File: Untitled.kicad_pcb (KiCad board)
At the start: 2 copper layers, 111.8 x 37.5 mm, 28 parts, among them J1 JAMMA, J2 CONN_01X06, J5 PWR_IN, J6 DC2DC, J7 SCART-F, SW1 SW_Push, SW2 SW_Push, SW3 SW_Push, U1 LD1117S33TR, U2 ESP32-WROOM, U3 TLC5926IDW, U4 TLC5926IDW

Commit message: Lynn almost done
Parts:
- removed C1, C2, C3: 4.7u, Capacitors_SMD:C_1206_HandSoldering
- removed J5: PWR_IN, Connectors:BARREL_JACK
- removed J6: DC2DC, NQR010A0X4Z:NQR010A0X4Z
- removed J7: SCART-F, w_conn_av:SCART
- removed R10: 100, Resistors_SMD:R_1206_HandSoldering
- removed R3, R4: 330, Resistors_SMD:R_1206_HandSoldering
- removed R5: 10K, Resistors_SMD:R_1206_HandSoldering
- removed R6: 1K, Resistors_SMD:R_1206_HandSoldering
- removed R7: 240, Resistors_SMD:R_1206_HandSoldering
- removed R8: 500, Potentiometers:Potentiometer_Bourns_3296W_3-8Zoll_Inline_ScrewUp
- removed R9: 33, Resistors_SMD:R_1206_HandSoldering
- removed SW1, SW2, SW3: SW_Push, Buttons_Switches_SMD:SW_SPST_EVQPE1
- added D1: LED, LEDs:LED_1206_HandSoldering, F.Cu at (241.2, 94.2)
- added D10: LED, LEDs:LED_1206_HandSoldering, F.Cu at (214.8, 100.2)
- added D11: LED, LEDs:LED_1206_HandSoldering, F.Cu at (231.2, 101.1)
- added D12: LED, LEDs:LED_1206_HandSoldering, F.Cu at (237.7, 98.7)
- added D13: LED, LEDs:LED_1206_HandSoldering, F.Cu at (223.1, 84.7)
- added D14: LED, LEDs:LED_1206_HandSoldering, F.Cu at (225.3, 78.6)
- added D15: LED, LEDs:LED_1206_HandSoldering, F.Cu at (205.2, 96.0)
- added D16: LED, LEDs:LED_1206_HandSoldering, F.Cu at (207.4, 89.8)
- added D17: LED, LEDs:LED_1206_HandSoldering, F.Cu at (197.5, 85.0)
- added D18: LED, LEDs:LED_1206_HandSoldering, F.Cu at (200.9, 78.7)
- added D19: LED, LEDs:LED_1206_HandSoldering, F.Cu at (205.2, 81.5)
- added D2: LED, LEDs:LED_1206_HandSoldering, F.Cu at (234.6, 78.6)
- added D20: LED, LEDs:LED_1206_HandSoldering, F.Cu at (210.6, 78.8)
- added D21: LED, LEDs:LED_1206_HandSoldering, F.Cu at (210.3, 84.9)
- added D22: LED, LEDs:LED_1206_HandSoldering, F.Cu at (195.7, 90.2)
- added D23: LED, LEDs:LED_1206_HandSoldering, F.Cu at (192.2, 96.0)
- added D24: LED, LEDs:LED_1206_HandSoldering, F.Cu at (185.2, 100.8)
- added D25: LED, LEDs:LED_1206_HandSoldering, F.Cu at (178.5, 104.0)
- added D26: LED, LEDs:LED_1206_HandSoldering, F.Cu at (170.2, 107.0)
- added D27: LED, LEDs:LED_1206_HandSoldering, F.Cu at (164.9, 113.2)
- added D28: LED, LEDs:LED_1206_HandSoldering, F.Cu at (165.4, 122.5)
- added D29: LED, LEDs:LED_1206_HandSoldering, F.Cu at (171.2, 117.5)
- added D3: LED, LEDs:LED_1206_HandSoldering, F.Cu at (229.4, 81.3)
- added D30: LED, LEDs:LED_1206_HandSoldering, F.Cu at (175.4, 110.5)
- added D31: LED, LEDs:LED_1206_HandSoldering, F.Cu at (180.7, 97.2)
- added D32: LED, LEDs:LED_1206_HandSoldering, F.Cu at (183.7, 91.0)
- added D33: LED, LEDs:LED_1206_HandSoldering, F.Cu at (186.7, 85.2)
- added D34: LED, LEDs:LED_1206_HandSoldering, F.Cu at (189.2, 79.2)
- added D35: LED, LEDs:LED_1206_HandSoldering, F.Cu at (172.2, 100.5)
- added D36: LED, LEDs:LED_1206_HandSoldering, F.Cu at (169.2, 94.0)
- added D37: LED, LEDs:LED_1206_HandSoldering, F.Cu at (172.7, 87.8)
- added D38: LED, LEDs:LED_1206_HandSoldering, F.Cu at (176.4, 80.8)
- added D39: LED, LEDs:LED_1206_HandSoldering, F.Cu at (160.7, 98.2)
- added D4: LED, LEDs:LED_1206_HandSoldering, F.Cu at (234.7, 84.3)
- added D40: LED, LEDs:LED_1206_HandSoldering, F.Cu at (150.7, 100.0)
- added D41: LED, LEDs:LED_1206_HandSoldering, F.Cu at (148.9, 93.5)
- added D42: LED, LEDs:LED_1206_HandSoldering, F.Cu at (152.2, 86.8)
- added D43: LED, LEDs:LED_1206_HandSoldering, F.Cu at (155.4, 80.8)
- added D44: LED, LEDs:LED_1206_HandSoldering, F.Cu at (159.7, 74.0)
- added D45: LED, LEDs:LED_1206_HandSoldering, F.Cu at (162.9, 68.0)
- added D46: LED, LEDs:LED_1206_HandSoldering, B.Cu at (159.2, 90.2)
- added D47: LED, LEDs:LED_1206_HandSoldering, B.Cu at (159.2, 87.2)
- added D48: LED, LEDs:LED_1206_HandSoldering, B.Cu at (159.2, 84.2)
- added D5: LED, LEDs:LED_1206_HandSoldering, F.Cu at (231.4, 89.2)
- added D6: LED, LEDs:LED_1206_HandSoldering, F.Cu at (229.4, 95.4)
- added D7: LED, LEDs:LED_1206_HandSoldering, F.Cu at (220.2, 89.2)
- added D8: LED, LEDs:LED_1206_HandSoldering, F.Cu at (217.4, 94.5)
- added D9: LED, LEDs:LED_1206_HandSoldering, F.Cu at (206.6, 100.9)
- added U5: TLC5926IDW, Housings_SOIC:SOIC-24W_7.5x15.4mm_Pitch1.27mm, B.Cu at (172.8, 87.8)
- added lynn_outline: G***, svg2mod:lynn_outline, F.Cu at (175.0, 85.2)
- C4, R2, U1, U2, U3: moved to B.Cu
- J1: value JAMMA -> USB_B; footprint JAMMA:JAMMA -> Connectors:USB_Mini-B; moved to B.Cu
- R1: value 330 -> 10K; moved to B.Cu
- R11: value R -> 330; moved to B.Cu
- R12: value R -> 330
- moved C4 146.5 mm to (235.8, 102.3), turned to 0 degrees
- moved J2 142.8 mm to (228.7, 75.3), turned to 270 degrees
- moved U2 138.0 mm to (234.9, 89.4)
- moved R11 99.3 mm to (205.6, 77.7), turned to 0 degrees
- moved U3 94.9 mm to (205.7, 87.6), turned to 180 degrees
- moved R12 86.5 mm to (189.0, 77.0), turned to 0 degrees
- moved U4 82.8 mm to (189.6, 87.5), turned to 180 degrees
- moved J1 77.4 mm to (195.9, 101.2), turned to 90 degrees
- moved R2 74.3 mm to (172.8, 77.5), turned to 0 degrees
- moved R1 73.1 mm to (228.3, 102.3), turned to 180 degrees
- moved U1 49.5 mm to (176.7, 113.5)
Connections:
- J1 pad 1: GND -> +5V
- J1 pad 2: GND -> (no net)
- J1 pad 3: GND -> (no net)
- J1 pad 5: +5V -> (no net)
- J1 pad 6: +5V -> (no net)
- J2 pad 1: (no net) -> RESET
- J2 pad 5: (no net) -> PROG
- R1 pad 1: Net-(J7-Pad19) -> 33
- R1 pad 2: SYNC -> RESET
- R2 pad 2: Net-(C1-Pad2) -> GND
- U2 pad 25: Net-(SW3-Pad1) -> PROG
- U2 pad 29: LATCH -> (no net)
- U2 pad 3: Net-(SW2-Pad2) -> RESET
- U2 pad 30: CLK -> LATCH
- U2 pad 31: (no net) -> CLK
- U3 pad 10: LEFT1 -> Net-(D6-Pad1)
- U3 pad 11: DOWN1 -> Net-(D7-Pad1)
- U3 pad 12: UP1 -> Net-(D8-Pad1)
- U3 pad 13: TEST -> Net-(D9-Pad1)
- U3 pad 14: COIN1 -> Net-(D10-Pad1)
- U3 pad 15: START1 -> Net-(D11-Pad1)
- U3 pad 16: (no net) -> Net-(D12-Pad1)
- U3 pad 17: (no net) -> Net-(D13-Pad1)
- U3 pad 18: (no net) -> Net-(D14-Pad1)
- U3 pad 19: (no net) -> Net-(D15-Pad1)
- U3 pad 20: (no net) -> Net-(D16-Pad1)
- U3 pad 5: D1 -> Net-(D1-Pad1)
- U3 pad 6: C1 -> Net-(D2-Pad1)
- U3 pad 7: B1 -> Net-(D3-Pad1)
- U3 pad 8: A1 -> Net-(D4-Pad1)
- U3 pad 9: RIGHT1 -> Net-(D5-Pad1)
- U4 pad 10: START2 -> Net-(D22-Pad1)
- U4 pad 11: COIN2 -> Net-(D23-Pad1)
- U4 pad 12: SERVICE -> Net-(D24-Pad1)
- U4 pad 13: UP2 -> Net-(D25-Pad1)
- U4 pad 14: DOWN2 -> Net-(D26-Pad1)
- U4 pad 15: LEFT2 -> Net-(D27-Pad1)
- U4 pad 16: RIGHT2 -> Net-(D28-Pad1)
- U4 pad 17: A2 -> Net-(D29-Pad1)
- U4 pad 18: B2 -> Net-(D30-Pad1)
- U4 pad 19: C2 -> Net-(D31-Pad1)
- U4 pad 20: D2 -> Net-(D32-Pad1)
- U4 pad 22: (no net) -> Net-(U4-Pad22)
- U4 pad 5: (no net) -> Net-(D17-Pad1)
- U4 pad 6: (no net) -> Net-(D18-Pad1)
- U4 pad 7: (no net) -> Net-(D19-Pad1)
- U4 pad 8: (no net) -> Net-(D20-Pad1)
- U4 pad 9: (no net) -> Net-(D21-Pad1)
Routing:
- net +5V: track 126.2 -> 331.6 mm, vias 2 -> 3
- net GND: track 312.1 -> 162.7 mm, vias 5 -> 2
- net 33: track 77.8 -> 153.4 mm, vias 3 -> 0
- net +12V: track 69.1 -> 0.00 mm, vias 2 -> 0
- net Net-(D1-Pad1): track 0.00 -> 67.3 mm, vias 0 -> 1
- net RESET: track 0.00 -> 64.2 mm
- net Net-(D12-Pad1): track 0.00 -> 53.3 mm, vias 0 -> 1
- net VIDEO_GND: track 51.1 -> 0.00 mm, vias 2 -> 0
- net Net-(D28-Pad1): track 0.00 -> 45.3 mm, vias 0 -> 1
- net Net-(D29-Pad1): track 0.00 -> 43.7 mm, vias 0 -> 1
- net Net-(D44-Pad1): track 0.00 -> 37.4 mm, vias 0 -> 1
- net Net-(J6-Pad5): track 33.5 -> 0.00 mm, vias 1 -> 0
- net Net-(D11-Pad1): track 0.00 -> 32.9 mm, vias 0 -> 1
- net Net-(D27-Pad1): track 0.00 -> 32.5 mm, vias 0 -> 1
- net Net-(D5-Pad1): track 0.00 -> 31.5 mm, vias 0 -> 1
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- added copper zone on F.Cu, net +5V
- removed copper zone on F.Cu, net GND
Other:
- board size 111.8 x 37.5 mm -> 102 x 70.3 mm
- board text removed: "+"
- board text removed: "-"
- board text removed: "12V"
- board text removed: "5V Adjust"
- board text removed: "AUDIO"
- board text removed: "BLUE"
- board text removed: "Caution HOT"
- board text removed: "ESP32 PROGRAM"
- board text removed: "ESP32 RESET"
- board text removed: "GREEN"
- board text removed: "KEY"
- board text removed: "RED"
- board text removed: "RESET"
- board text removed: "SYNC"
- board text removed: "github.com/charcole/minigun"

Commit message: Lynn V1
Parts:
- removed J2: CONN_01X06, Pin_Headers:Pin_Header_Straight_1x06
- added TP1: TEST, Measurement_Points:Measurement_Point_Round-SMD-Pad_Small, B.Cu at (171.8, 113.0)
- added TP2: TEST, Measurement_Points:Measurement_Point_Square-SMD-Pad_Small, B.Cu at (239.6, 77.2)
- added TP3: TEST, Measurement_Points:Measurement_Point_Round-SMD-Pad_Small, B.Cu at (219.6, 102.3)
- added TP4: TEST, Measurement_Points:Measurement_Point_Round-SMD-Pad_Small, B.Cu at (222.9, 102.3)
- added TP5: TEST, Measurement_Points:Measurement_Point_Round-SMD-Pad_Small, B.Cu at (236.7, 77.1)
- added TP6: TEST, Measurement_Points:Measurement_Point_Round-SMD-Pad_Small, B.Cu at (234.1, 77.1)
- added TP7: TEST, Measurement_Points:Measurement_Point_Round-SMD-Pad_Small, B.Cu at (216.2, 80.4)
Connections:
- net RESET renamed Net-(R1-Pad2)
- J1 pad 2: (no net) -> Net-(J1-Pad2)
- J1 pad 3: (no net) -> Net-(J1-Pad3)
- J1 pad 5: (no net) -> Net-(J1-Pad5)
- U2 pad 10: (no net) -> Net-(U2-Pad10)
- U2 pad 11: (no net) -> Net-(U2-Pad11)
- U2 pad 12: (no net) -> Net-(U2-Pad12)
- U2 pad 13: (no net) -> Net-(U2-Pad13)
- U2 pad 14: (no net) -> Net-(U2-Pad14)
- U2 pad 16: (no net) -> Net-(U2-Pad16)
- U2 pad 17: (no net) -> Net-(U2-Pad17)
- U2 pad 18: (no net) -> Net-(U2-Pad18)
- U2 pad 19: (no net) -> Net-(U2-Pad19)
- U2 pad 20: (no net) -> Net-(U2-Pad20)
- U2 pad 21: (no net) -> Net-(U2-Pad21)
- U2 pad 22: (no net) -> Net-(U2-Pad22)
- U2 pad 23: (no net) -> Net-(U2-Pad23)
- U2 pad 24: (no net) -> Net-(U2-Pad24)
- U2 pad 25: PROG -> Net-(TP7-Pad1)
- U2 pad 26: (no net) -> Net-(U2-Pad26)
- U2 pad 29: (no net) -> Net-(U2-Pad29)
- U2 pad 32: (no net) -> Net-(U2-Pad32)
- U2 pad 33: (no net) -> Net-(U2-Pad33)
- U2 pad 36: (no net) -> Net-(U2-Pad36)
- U2 pad 37: (no net) -> Net-(U2-Pad37)
- U2 pad 4: (no net) -> Net-(U2-Pad4)
- U2 pad 5: (no net) -> Net-(U2-Pad5)
- U2 pad 6: (no net) -> Net-(U2-Pad6)
- U2 pad 7: (no net) -> Net-(U2-Pad7)
- U2 pad 8: (no net) -> Net-(U2-Pad8)
- U2 pad 9: (no net) -> Net-(U2-Pad9)
- U5 pad 22: (no net) -> Net-(U5-Pad22)
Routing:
- net GND: track 162.7 -> 313.1 mm
- net 33: track 153.4 -> 221.8 mm, vias 0 -> 4
- net Net-(R1-Pad2): track 64.2 -> 16.9 mm
- net Net-(D2-Pad1): track 0.00 -> 34.7 mm, vias 0 -> 3
- net Net-(D1-Pad1): track 67.3 -> 46.8 mm, vias 1 -> 3
- net CLK: track 48.2 -> 65.4 mm, vias 0 -> 2
- net Net-(TP6-Pad1): track 14.2 -> 3.71 mm
- net PROG: track 9.58 -> 0.00 mm, vias 1 -> 0
- net Net-(TP5-Pad1): track 13.6 -> 4.34 mm
- net Net-(TP7-Pad1): track 0.00 -> 7.46 mm
- net +5V: track 331.6 -> 337.9 mm
- net LATCH: track 58.4 -> 60.4 mm
- net Net-(D14-Pad1): track 28.5 -> 26.7 mm, vias 3 -> 1
- net Net-(D31-Pad1): track 14.9 -> 13.2 mm
- net Net-(D12-Pad1): track 53.3 -> 52.1 mm

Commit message: Finished board?
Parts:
- moved U2 4.37 mm to (230.6, 89.4)
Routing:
- net +5V: track 337.9 -> 345.6 mm
- net Net-(D5-Pad1): track 31.5 -> 37.9 mm
- net LATCH: track 60.4 -> 54.9 mm
- net CLK: track 65.4 -> 60.1 mm
- net OE: track 65.6 -> 60.7 mm
- net Net-(TP7-Pad1): track 7.46 -> 3.09 mm
- net Net-(R1-Pad2): track 16.9 -> 12.5 mm
- net DATA: track 18.4 -> 14.3 mm
- net Net-(D13-Pad1): track 23.0 -> 27.0 mm
- net 33: track 221.8 -> 218.3 mm
- net Net-(TP5-Pad1): track 4.34 -> 6.42 mm
- net Net-(D2-Pad1): track 34.7 -> 32.8 mm
- net GND: track 313.1 -> 311.4 mm
- net Net-(TP6-Pad1): track 3.71 -> 5.32 mm
- net Net-(D7-Pad1): track 10.7 -> 9.85 mm
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
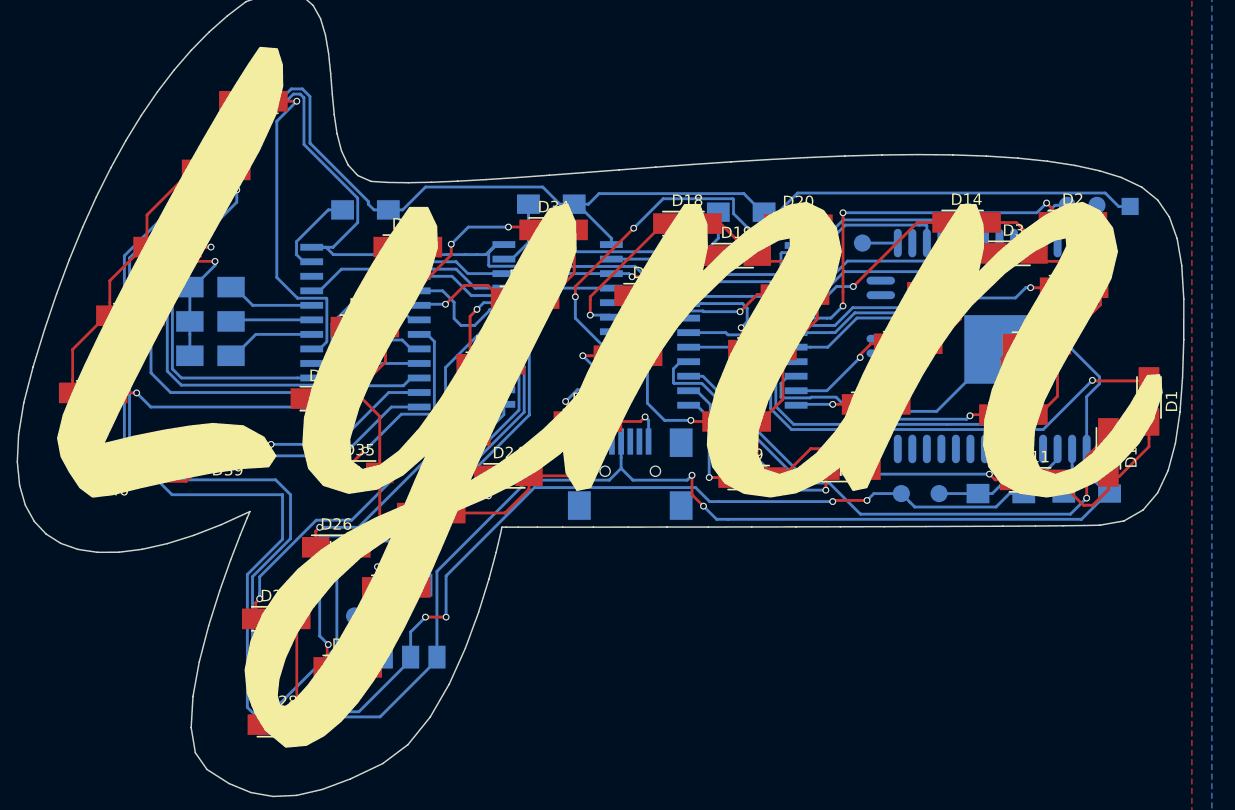
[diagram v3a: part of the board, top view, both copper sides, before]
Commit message: Increased power line thickness
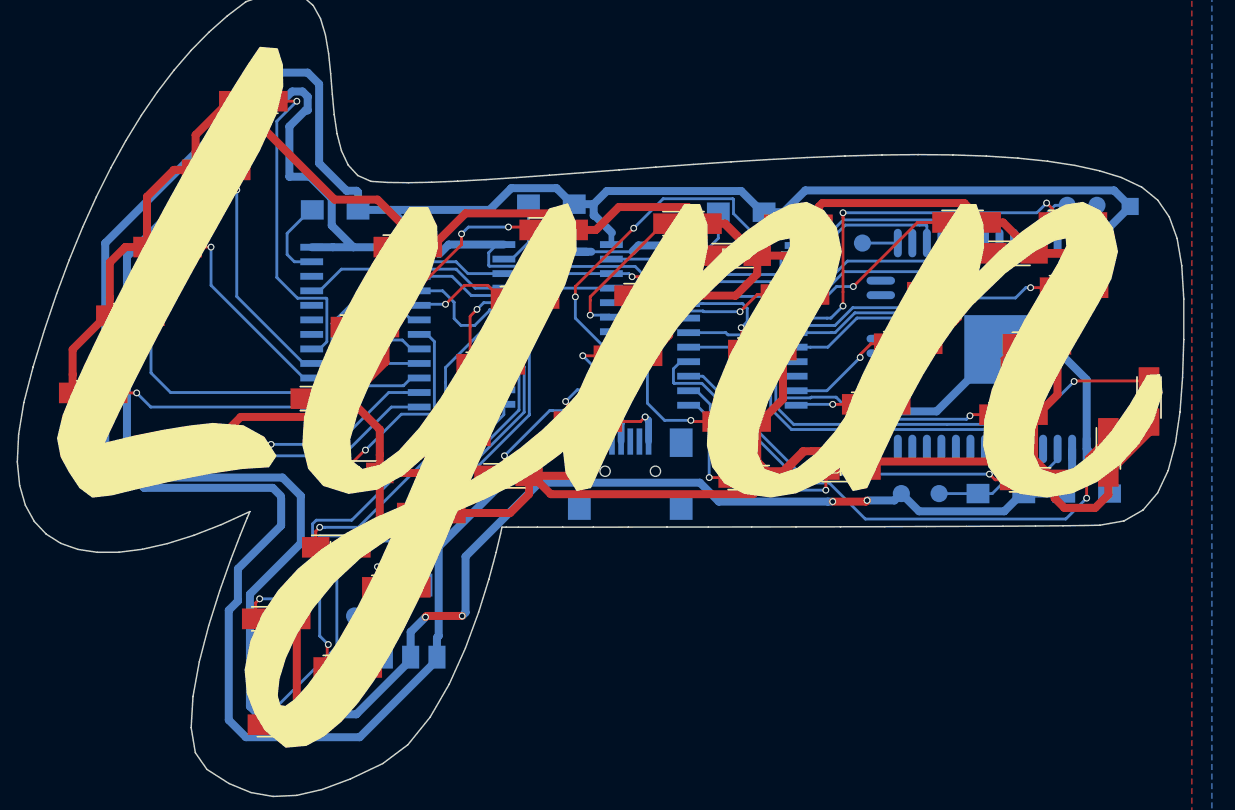
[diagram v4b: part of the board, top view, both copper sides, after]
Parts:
- removed D46, D47, D48: LED, LEDs:LED_1206_HandSoldering
- moved R2 2.65 mm to (170.1, 77.5)
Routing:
- net +5V: track 345.6 -> 541.2 mm, vias 3 -> 2
- net GND: track 311.4 -> 289.3 mm, vias 2 -> 0
- net Net-(D44-Pad1): track 37.4 -> 20.0 mm
- net Net-(D43-Pad1): track 27.2 -> 17.5 mm
- net 33: track 218.3 -> 227.2 mm
- net Net-(D46-Pad1): track 7.82 -> 0.00 mm
- net Net-(D48-Pad1): track 7.71 -> 0.00 mm
- net Net-(D47-Pad1): track 7.11 -> 0.00 mm
- net Net-(D24-Pad1): track 15.8 -> 13.7 mm
- net Net-(D27-Pad1): track 32.5 -> 33.5 mm
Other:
- net class Power added: clearance 0.2, trace_width 0.5, via_dia 0.6, via_drill 0.4

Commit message: Made shorter to fit within limits
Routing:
- net 33: track 227.2 -> 221.8 mm
- net GND: track 289.3 -> 284.1 mm
- net Net-(D45-Pad1): track 28.6 -> 26.0 mm
- net Net-(D27-Pad1): track 33.5 -> 32.6 mm
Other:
- board size 102 x 70.3 mm -> 99.5 x 68.9 mm
- net class Power: trace_width 0.5 -> 0.7
